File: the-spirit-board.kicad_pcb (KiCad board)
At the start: 2 copper layers, 25 x 23 mm, 45 parts, among them IC1 ESP32-C6-WROOM-1-N8, IC2 AP2112K-3.3TRG1, Q1 BSS138, Q2 BSS138, Q3 BSS138, Q4 BSS138, Q5 BSS138, Q6 BSS138, Q7 BSS138

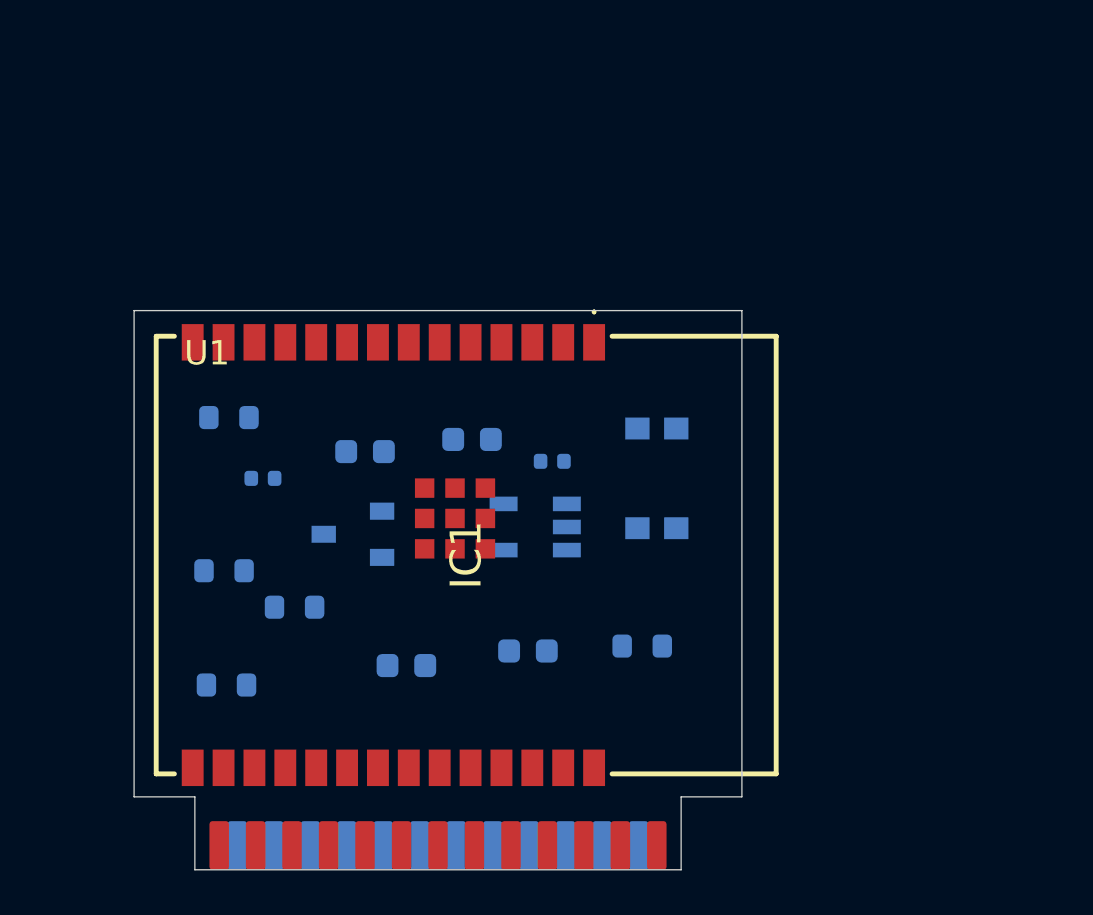
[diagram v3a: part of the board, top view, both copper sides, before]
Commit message: Add USB-C connection
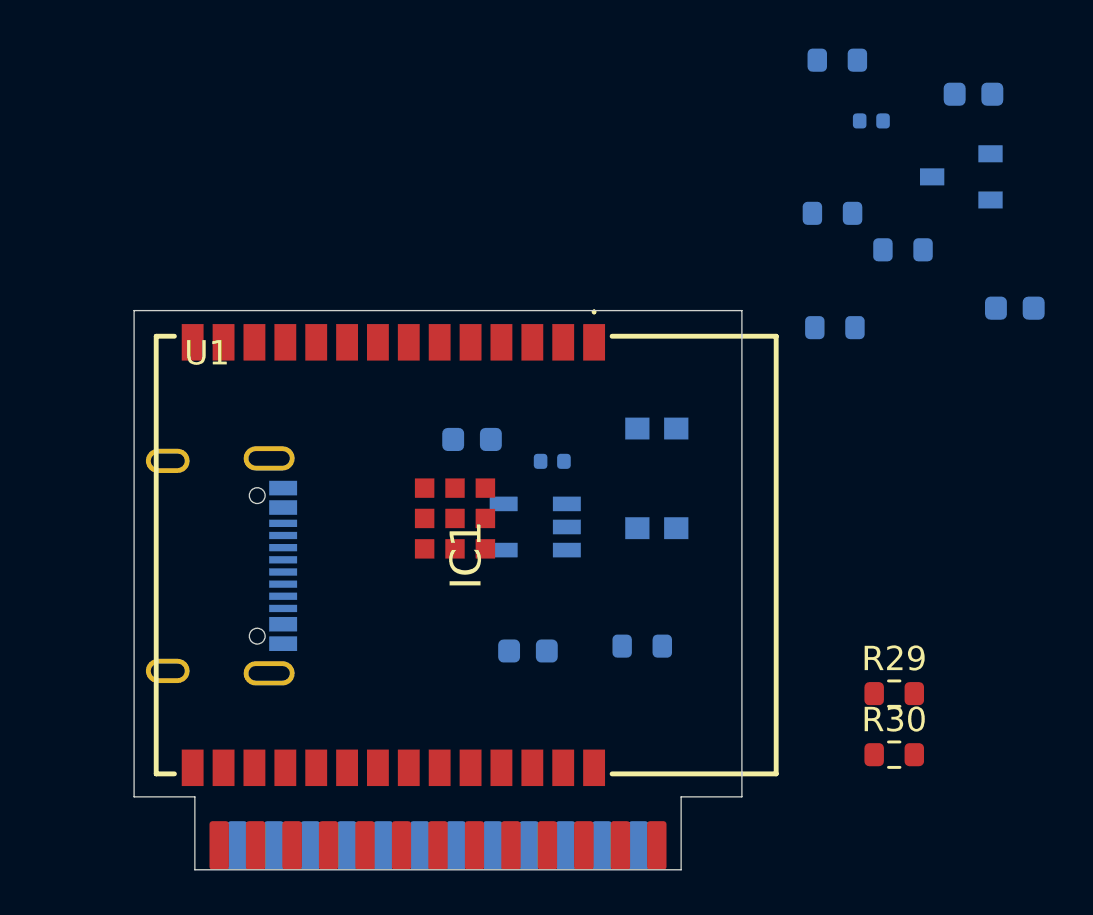
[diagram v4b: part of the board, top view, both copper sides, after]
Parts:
- added J1: RAHUC31AUTR, TheSPIRITBoard:RAHUC31AUTR, B.Cu at (145.1, 132.5)
- added R29: 5.1k, Resistor_SMD:R_0603_1608Metric, F.Cu at (171.3, 137.8)
- added R30: 5.1k, Resistor_SMD:R_0603_1608Metric, F.Cu at (171.3, 140.3)
- moved C5 29.0 mm to (174.5, 113.1)
- moved R3 29.0 mm to (168.9, 111.7)
- moved C6 29.0 mm to (176.2, 121.9)
- moved Q1 29.0 mm to (174.0, 116.5)
- moved R2 29.0 mm to (171.6, 119.5)
- moved R5 29.0 mm to (168.7, 118.0)
- moved C3 29.0 mm to (170.3, 114.2)
- moved R4 29.0 mm to (168.8, 122.7)

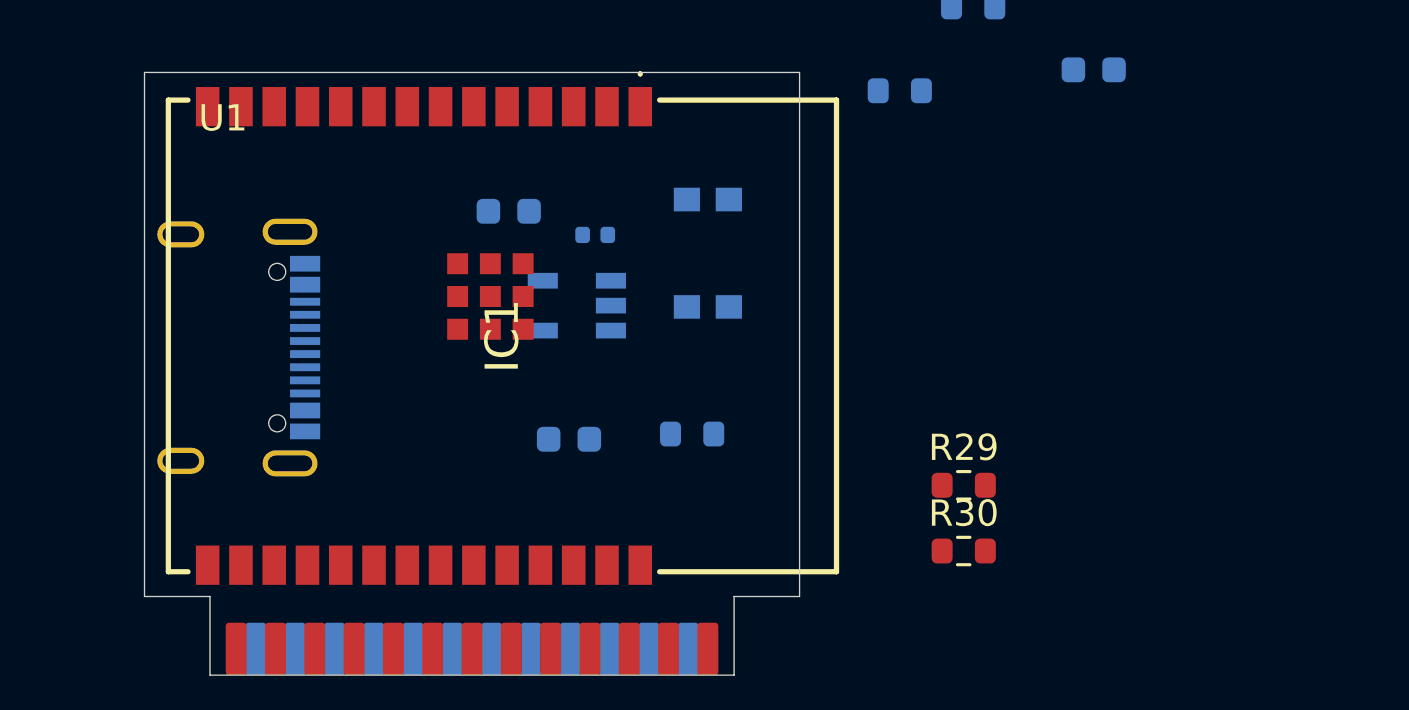
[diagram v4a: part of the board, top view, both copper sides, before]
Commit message: Add an I2S microphone module
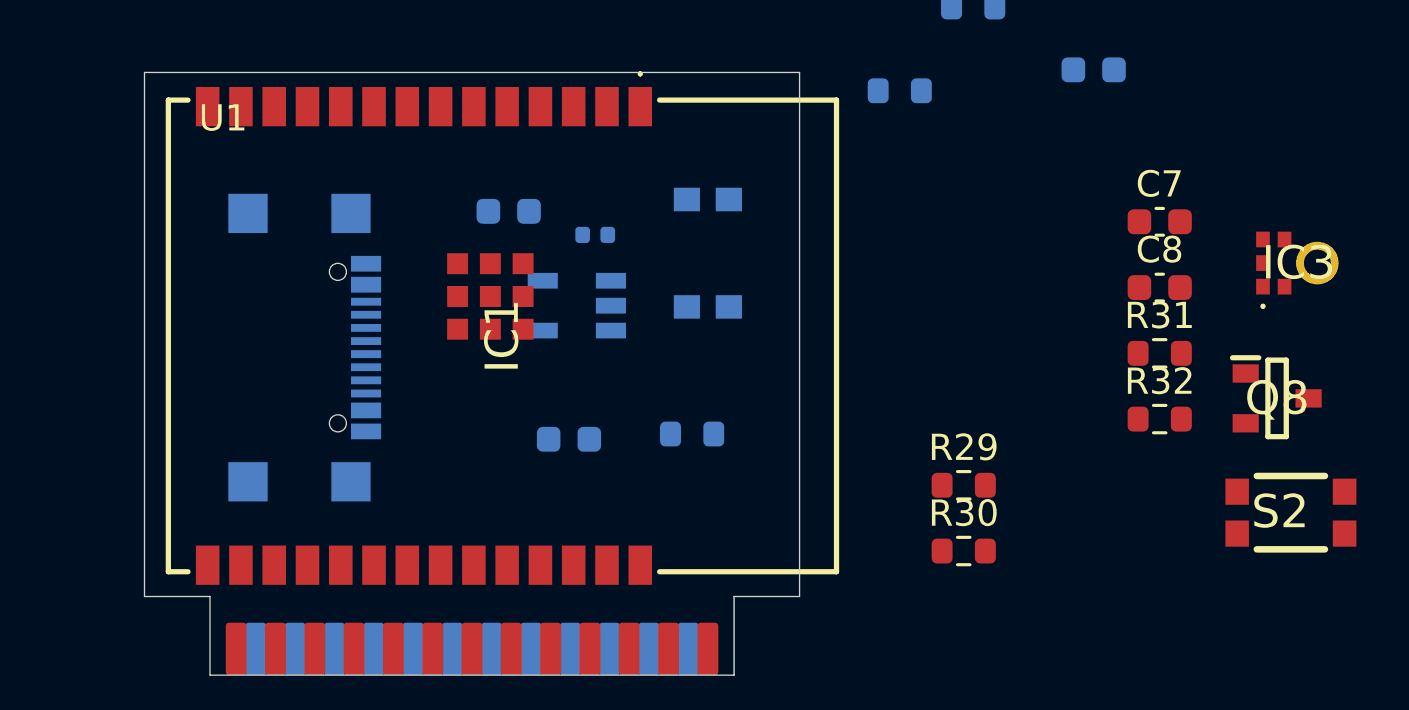
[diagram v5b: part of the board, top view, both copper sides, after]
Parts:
- added C7: 0.1uF, Capacitor_SMD:C_0603_1608Metric, F.Cu at (178.7, 127.7)
- added C8: 1uF, Capacitor_SMD:C_0603_1608Metric, F.Cu at (178.7, 130.2)
- added IC3: ICS-43434, TheSPIRITBoard:ICS43434, F.Cu at (184.1, 129.3)
- added Q8: BSS138, TheSPIRITBoard:SOT95P240X120-3N, F.Cu at (183.2, 134.4)
- added R31: 10k, Resistor_SMD:R_0603_1608Metric, F.Cu at (178.7, 132.7)
- added R32: 10k, Resistor_SMD:R_0603_1608Metric, F.Cu at (178.7, 135.2)
- added S2: KMR211G_LFS, TheSPIRITBoard:KMR_2, F.Cu at (183.8, 138.8)
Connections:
- IC1 pad 15: /IO9 -> GND
- Q7 pad 2: /IO9 -> GND
- R27 pad 2: /IO9 -> GND
- U1 pad 6: /GEAR_LED -> //POWER_DOWN

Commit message: Initial draft of the schematic complete
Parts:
- added D1: B340A-E3/61T, Diode_SMD:D_SMA, F.Cu at (184.0, 114.8)
- added D2: LED, LED_SMD:LED_0603_1608Metric, F.Cu at (186.0, 122.9)
- added Q9: DMG3415U-7, TheSPIRITBoard:SOT96P240X110-3N, F.Cu at (186.3, 119.3)
- added R33: 100k, Resistor_SMD:R_0603_1608Metric, F.Cu at (182.0, 118.3)
- added R34: 5.1k, Resistor_SMD:R_0603_1608Metric, F.Cu at (182.0, 120.8)
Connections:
- C5 pad 2: +5.31V -> Net-(D1-K)
- IC2 pad 1: +5.31V -> Net-(D1-K)
- J1 pad A6: Net-(J1-DP1) -> /IO13
- J1 pad A7: Net-(J1-DN1) -> /IO12
- J1 pad B6: Net-(J1-DP1) -> /IO13
- J1 pad B7: Net-(J1-DN1) -> /IO12
- R2 pad 1: +5.31V -> Net-(D1-K)

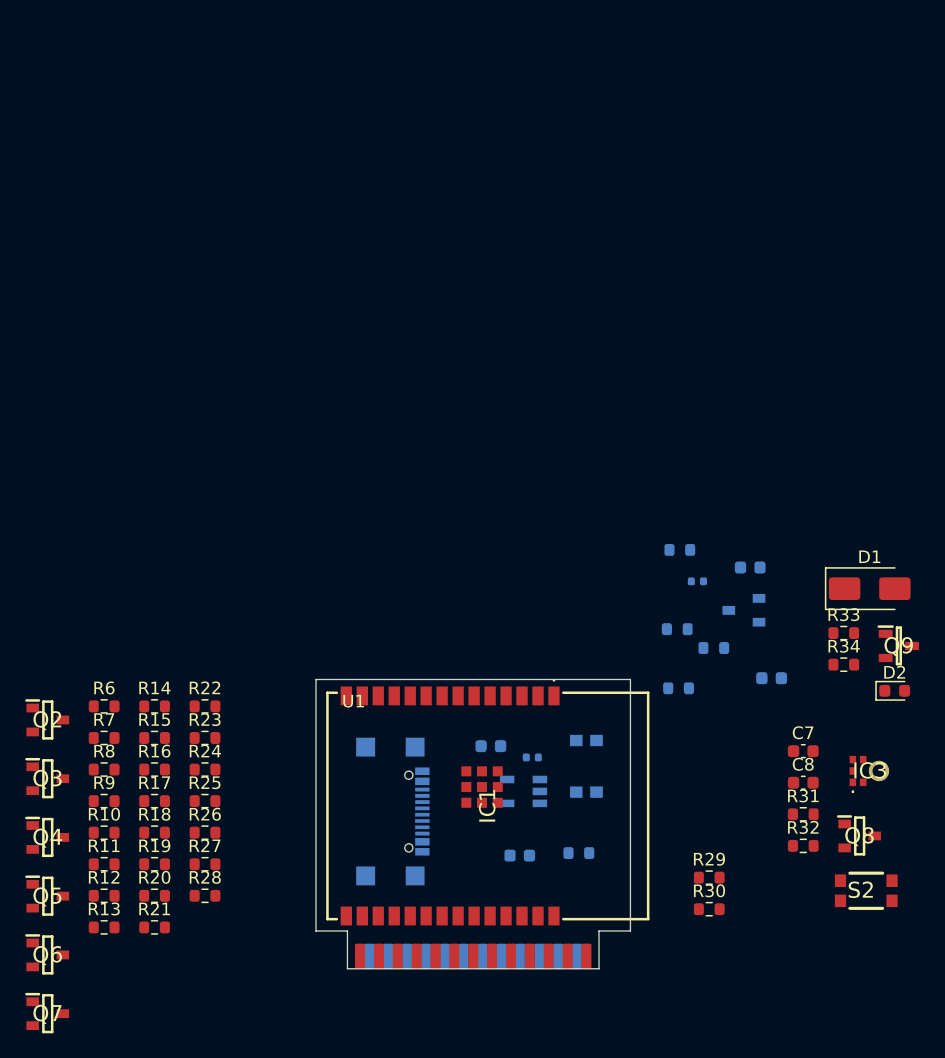
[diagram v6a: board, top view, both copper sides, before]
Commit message: Lots of updates to the PCB; all connections made except for one diode; working on passing DRC; targeting 4pcb
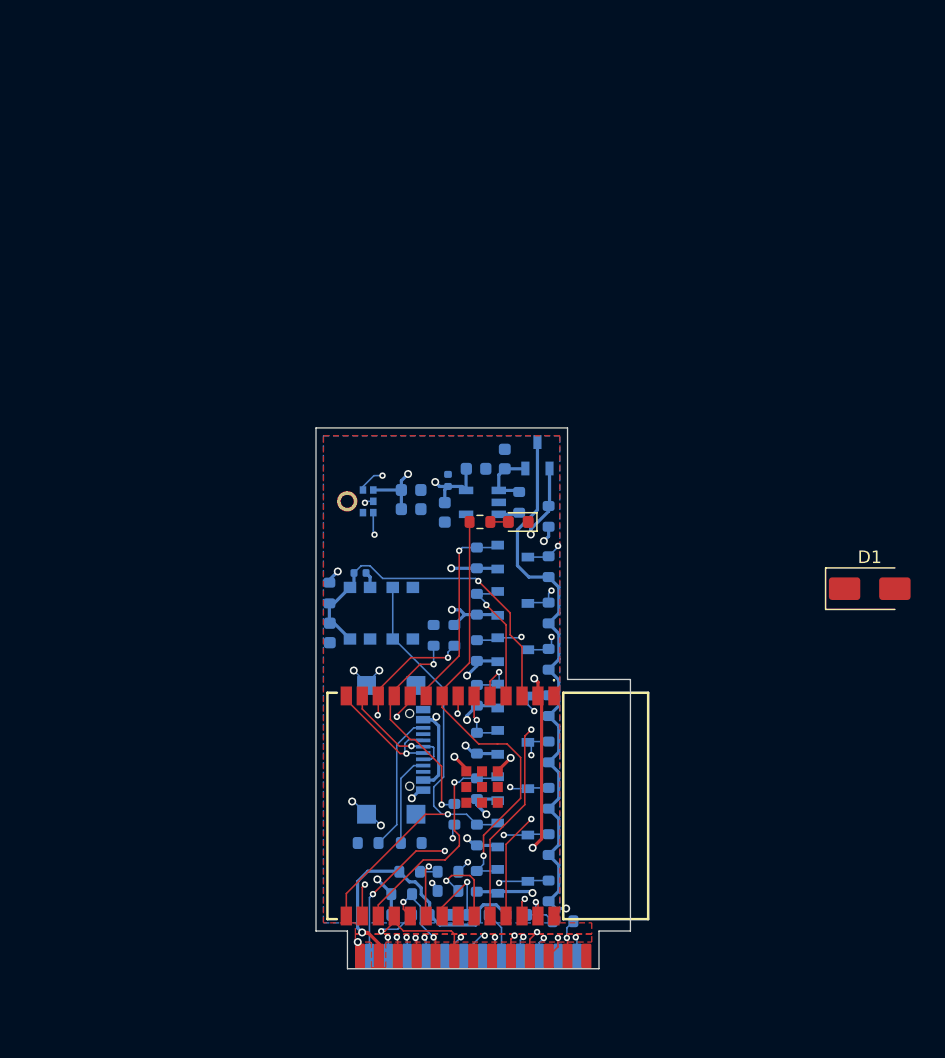
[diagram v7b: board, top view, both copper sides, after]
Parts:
- C7, C8, IC3, Q2, Q3, Q4, Q5, Q6, Q7, Q8, Q9, R10, R11, R12, R13, R14, R15, R16, R17, R18, R19, R20, R21, R22, R23, R24, R25, R26, R27, R28, R29, R30, R31, R32, R33, R6, R7, R8, R9, S2: moved to B.Cu
- moved IC3 46.1 mm to (143.2, 107.8), turned to 180 degrees
- moved S2 43.0 mm to (146.9, 116.7), turned to -90 degrees
- moved R11 42.5 mm to (158.5, 113.0), turned to 90 degrees
- moved Q4 41.4 mm to (155.6, 116.0)
- moved Q6 40.6 mm to (155.6, 127.0)
- moved Q5 40.2 mm to (155.6, 123.3)
- moved Q7 39.6 mm to (155.6, 134.4)
- moved Q2 39.2 mm to (155.6, 112.3)
- moved Q3 38.4 mm to (155.6, 119.6)
- moved C8 38.0 mm to (147.6, 108.5), turned to 180 degrees
- moved C7 37.5 mm to (147.6, 106.9), turned to 180 degrees
- moved R10 36.8 mm to (152.8, 112.3), turned to 90 degrees
- moved R12 36.5 mm to (159.6, 141.2), turned to 180 degrees
- moved R17 34.7 mm to (158.5, 116.7), turned to 90 degrees
- moved R21 34.3 mm to (158.5, 127.8), turned to 90 degrees
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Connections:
- IC1 pad 15: GND -> /IO9
- Q7 pad 2: GND -> /IO9
- R27 pad 2: GND -> /IO9
- S2 pad 2: Net-(S2-Pad2) -> /IO9
- S2 pad 4: Net-(S2-Pad2) -> /IO9
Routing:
- net +5.31V: track 0.00 -> 67.9 mm, vias 0 -> 2
- net +3.3V: track 0.00 -> 58.8 mm, vias 0 -> 15
- net /TXD0: track 0.00 -> 43.4 mm, vias 0 -> 2
- net /RXD0: track 0.00 -> 38.6 mm, vias 0 -> 2
- net /IO9: track 0.00 -> 37.7 mm, vias 0 -> 1
- net GND: track 0.00 -> 36.2 mm, vias 0 -> 9
- net //CTS: track 0.00 -> 36.1 mm, vias 0 -> 2
- net /IO0: track 0.00 -> 35.7 mm, vias 0 -> 1
- net /IO18: track 0.00 -> 33.7 mm, vias 0 -> 2
- net /D1: track 0.00 -> 32.5 mm, vias 0 -> 2
- net V_USB: track 0.00 -> 31.3 mm, vias 0 -> 2
- net /IO11: track 0.00 -> 29.6 mm, vias 0 -> 3
- net /D0: track 0.00 -> 28.6 mm, vias 0 -> 2
- net /EN: track 0.00 -> 28.4 mm, vias 0 -> 1
- net /IO3: track 0.00 -> 26.0 mm, vias 0 -> 2
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- added copper zone on In1.Cu, net +3.3V
- added copper zone on In2.Cu, net +3.3V
- added copper zone on B.Cu, net GND
- added copper zone on F.Cu, net GND
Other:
- board size 25 x 23 mm -> 25 x 43 mm
- copper layers 2 -> 4

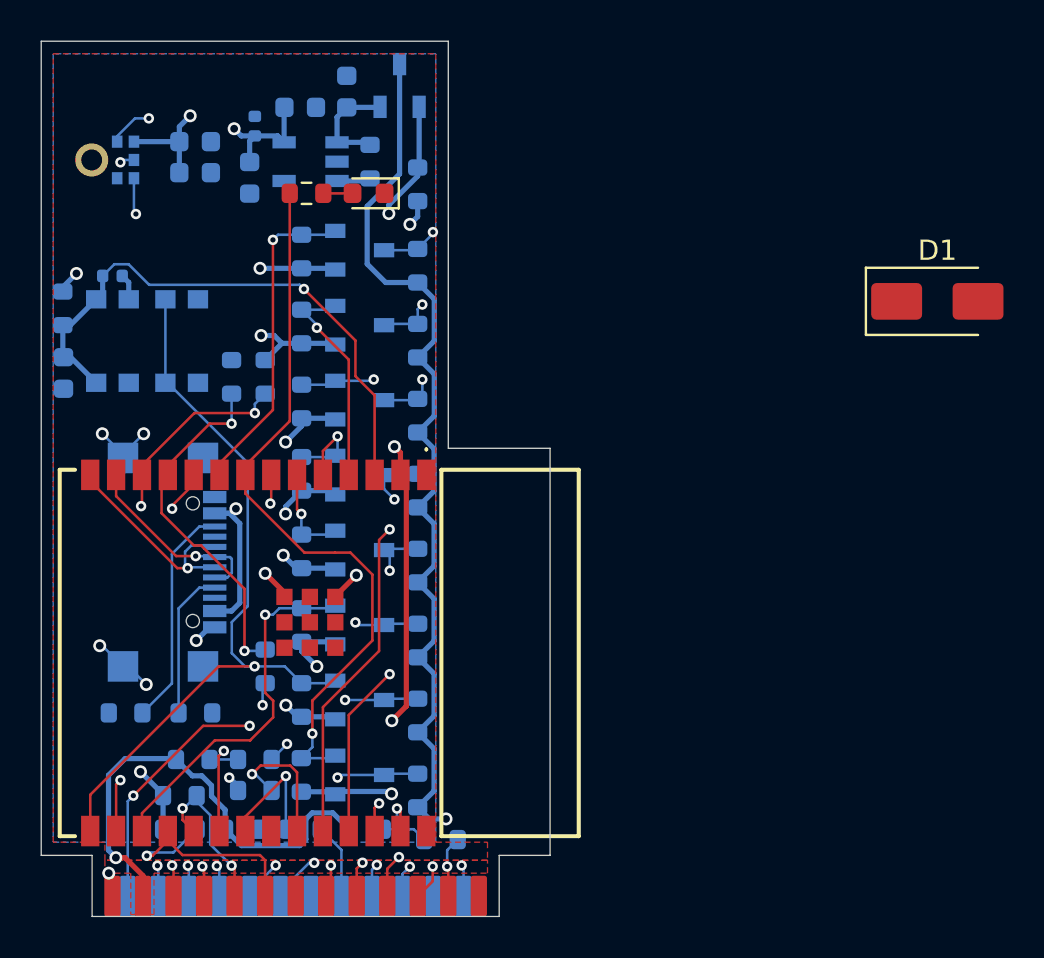
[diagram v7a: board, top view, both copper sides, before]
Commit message: Update the diode in the power supply
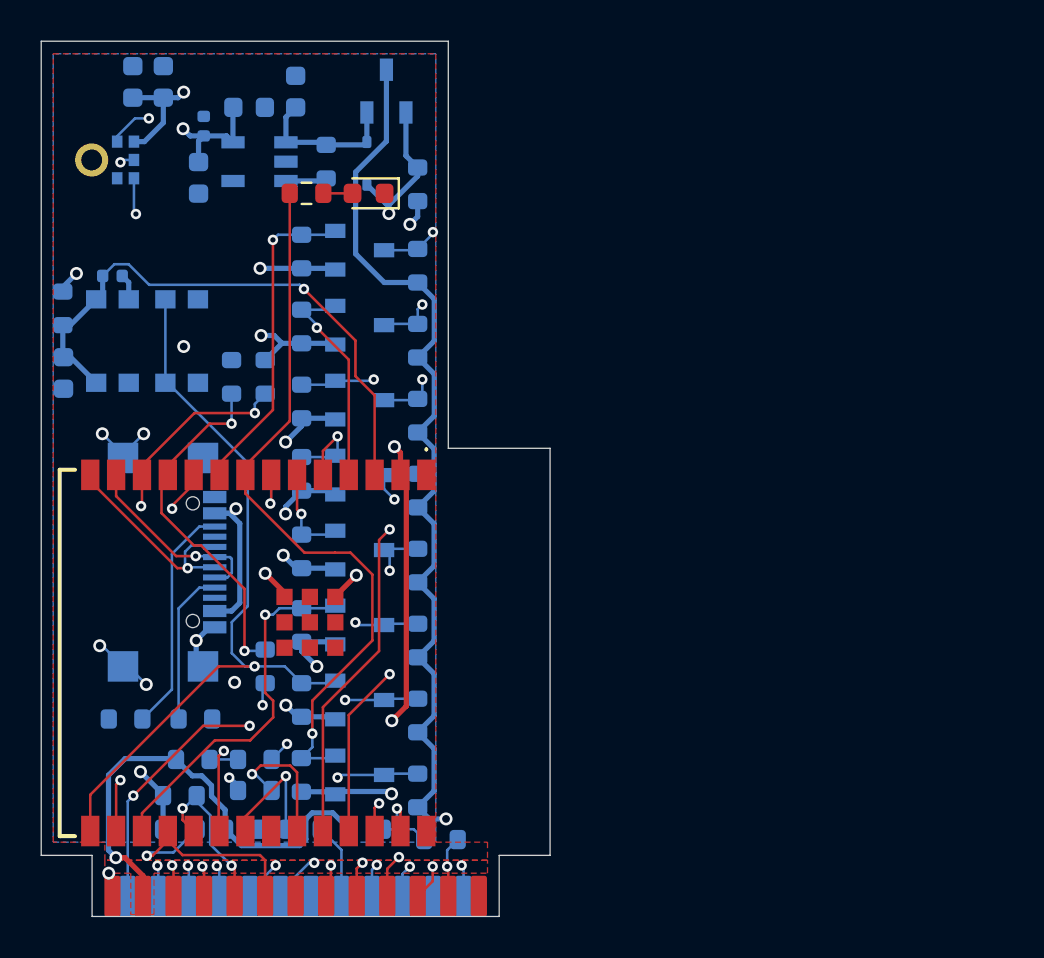
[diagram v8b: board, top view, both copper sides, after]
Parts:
- D1: value B340A-E3/61T -> B0530WSHE3-TP; footprint Diode_SMD:D_SMA -> Diode_SMD:D_SOD-323; moved to B.Cu
- moved D1 28.8 mm to (156.0, 108.0), turned to -90 degrees
- moved C8 5.41 mm to (144.5, 104.0), turned to -90 degrees
- moved C7 3.32 mm to (146.0, 104.0), turned to -90 degrees
- moved C4 2.51 mm to (147.7, 108.7)
- moved C3 2.51 mm to (148.0, 106.2)
- moved C5 2.51 mm to (152.5, 104.5)
- moved C6 2.51 mm to (150.2, 105.2)
- moved IC2 2.51 mm to (150.7, 107.9)
- moved R2 2.15 mm to (154.0, 107.9)
- moved Q9 0.70 mm to (157.0, 104.5)
- moved R29 0.30 mm to (147.6, 135.3)
- moved R30 0.30 mm to (144.1, 135.3)
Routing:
- net GND: track 36.2 -> 48.2 mm, vias 9 -> 11
- net Net-(D1-K): track 5.23 -> 7.45 mm
- net V_USB: track 31.3 -> 32.8 mm
